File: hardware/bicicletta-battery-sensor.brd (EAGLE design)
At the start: 45.7 x 19.1 mm, 15 parts, among them IC1 LMP92064, IC2 TXB0108

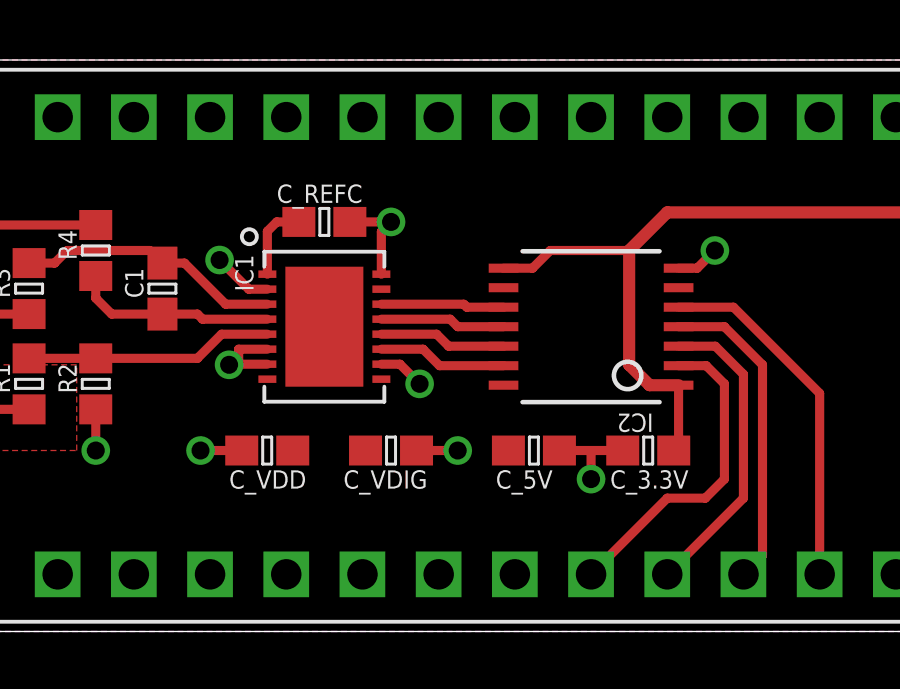
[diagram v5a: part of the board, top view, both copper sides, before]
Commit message: A little more space on the resistors for ease of soldering
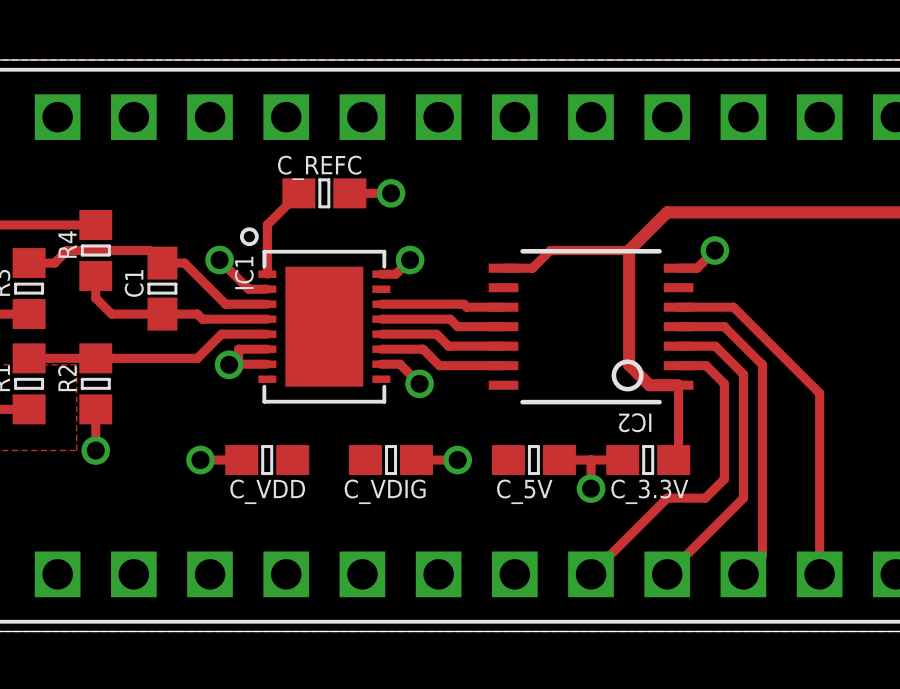
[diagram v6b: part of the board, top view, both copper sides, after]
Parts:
- moved C_REFC 0.95 mm to (19.1, 14.6)
- moved C_3.3V 0.32 mm to (29.8, 5.71)
- moved C_5V 0.32 mm to (26.0, 5.71)
- moved C_VDD 0.32 mm to (17.1, 5.71)
- moved C_VDIG 0.32 mm to (21.3, 5.71)
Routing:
- net REFC: track 2.61 -> 3.13 mm
- net GND: track 18.2 -> 17.9 mm, vias 9 -> 10
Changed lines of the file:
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@@
 <attribute name="VALUE" x="17.05" y="6.16" size="0.8128" layer="27"/>
 </element>
-<element name="C_REFC" library="rcl" package="C0603" value="1uF" x="19.05" y="13.6525" smashed="yes">
-<attribute name="NAME" x="17.4625" y="14.2875" size="0.6096" layer="25"/>
-<attribute name="VALUE" x="18.415" y="11.7475" size="1.27" layer="27"/>
-</element>
-<element name="C_VDD" library="rcl" package="C0603" value="0.1uF" x="17.145" y="6.0325" smashed="yes" rot="R180">
-<attribute name="NAME" x="15.875" y="4.7625" size="0.6096" layer="25"/>
-<attribute name="VALUE" x="17.78" y="7.9375" size="1.27" layer="27" rot="R180"/>
-</element>
-<element name="C_VDIG" library="rcl" package="C0603" value="0.1uF" x="21.2725" y="6.0325" smashed="yes">
-<attribute name="NAME" x="19.685" y="4.7625" size="0.6096" layer="25"/>
-<attribute name="VALUE" x="20.6375" y="4.1275" size="1.27" layer="27"/>
+<element name="C_REFC" library="rcl" package="C0603" value="1uF" x="19.05" y="14.605" smashed="yes">
+<attribute name="NAME" x="17.4625" y="15.24" size="0.6096" layer="25"/>
+<attribute name="VALUE" x="18.415" y="12.7" size="1.27" layer="27"/>
+</element>
+<element name="C_VDD" library="rcl" package="C0603" value="0.1uF" x="17.145" y="5.715" smashed="yes" rot="R180">
+<attribute name="NAME" x="15.875" y="4.445" size="0.6096" layer="25"/>
+<attribute name="VALUE" x="17.78" y="7.62" size="1.27" layer="27" rot="R180"/>
+</element>
+<element name="C_VDIG" library="rcl" package="C0603" value="0.1uF" x="21.2725" y="5.715" smashed="yes">
+<attribute name="NAME" x="19.685" y="4.445" size="0.6096" layer="25"/>
+<attribute name="VALUE" x="20.6375" y="3.81" size="1.27" layer="27"/>
 </element>
 <element name="R3" library="rcl" package="R0603" value="100" x="9.2075" y="11.43" smashed="yes" rot="R90">
@@
 <attribute name="VALUE" x="30.0228" y="14.0462" size="1.016" layer="27" ratio="10" rot="R180"/>
 </element>
-<element name="C_3.3V" library="rcl" package="C0603" value="0.1uF" x="29.845" y="6.0325" smashed="yes" rot="R180">
-<attribute name="NAME" x="28.575" y="4.7625" size="0.6096" layer="25"/>
-<attribute name="VALUE" x="30.48" y="7.9375" size="1.27" layer="27" rot="R180"/>
-</element>
-<element name="C_5V" library="rcl" package="C0603" value="0.1uF" x="26.035" y="6.0325" smashed="yes">
-<attribute name="NAME" x="24.765" y="4.7625" size="0.6096" layer="25"/>
-<attribute name="VALUE" x="25.4" y="4.1275" size="1.27" layer="27"/>
+<element name="C_3.3V" library="rcl" package="C0603" value="0.1uF" x="29.845" y="5.715" smashed="yes" rot="R180">
+<attribute name="NAME" x="28.575" y="4.445" size="0.6096" layer="25"/>
+<attribute name="VALUE" x="30.48" y="7.62" size="1.27" layer="27" rot="R180"/>
+</element>
+<element name="C_5V" library="rcl" package="C0603" value="0.1uF" x="26.035" y="5.715" smashed="yes">
+<attribute name="NAME" x="24.765" y="4.445" size="0.6096" layer="25"/>
+<attribute name="VALUE" x="25.4" y="3.81" size="1.27" layer="27"/>
 </element>
 </elements>
@@
 <wire x1="16.1925" y1="8.91" x2="16.1925" y2="9.41" width="0.3048" layer="1"/>
 <via x="15.875" y="8.89" extent="1-16" drill="0.6"/>
-<via x="14.9225" y="6.0325" extent="1-16" drill="0.6"/>
-<via x="23.495" y="6.0325" extent="1-16" drill="0.6"/>
-<via x="27.94" y="5.08" extent="1-16" drill="0.6"/>
+<via x="14.9225" y="5.715" extent="1-16" drill="0.6"/>
+<via x="23.495" y="5.715" extent="1-16" drill="0.6"/>
+<via x="27.94" y="4.7625" extent="1-16" drill="0.6"/>
 <via x="32.0675" y="12.7" extent="1-16" drill="0.6"/>
-<via x="21.2725" y="13.6525" extent="1-16" drill="0.6"/>
+<via x="21.9075" y="12.3825" extent="1-16" drill="0.6"/>
 <via x="11.43" y="6.0325" extent="1-16" drill="0.6"/>
 <wire x1="11.43" y1="7.405" x2="11.43" y2="6.0325" width="0.3048" layer="1"/>
 <wire x1="16.1925" y1="8.91" x2="15.875" y2="8.91" width="0.3048" layer="1"/>
 <wire x1="15.875" y1="8.91" x2="15.875" y2="8.89" width="0.3048" layer="1"/>
-<wire x1="16.295" y1="6.0325" x2="14.9225" y2="6.0325" width="0.3048" layer="1"/>
-<wire x1="22.1225" y1="6.0325" x2="23.495" y2="6.0325" width="0.3048" layer="1"/>
+<wire x1="16.295" y1="5.715" x2="14.9225" y2="5.715" width="0.3048" layer="1"/>
+<wire x1="22.1225" y1="5.715" x2="23.495" y2="5.715" width="0.3048" layer="1"/>
 <via x="22.225" y="8.255" extent="1-16" drill="0.6"/>
 <wire x1="20.95" y1="8.91" x2="21.57" y2="8.91" width="0.3048" layer="1"/>
 <wire x1="21.57" y1="8.91" x2="22.225" y2="8.255" width="0.3048" layer="1"/>
-<wire x1="26.885" y1="6.0325" x2="27.94" y2="6.0325" width="0.3048" layer="1"/>
-<wire x1="27.94" y1="6.0325" x2="28.995" y2="6.0325" width="0.3048" layer="1"/>
-<wire x1="27.94" y1="5.08" x2="27.94" y2="6.0325" width="0.3048" layer="1"/>
+<wire x1="26.885" y1="5.715" x2="27.94" y2="5.715" width="0.3048" layer="1"/>
+<wire x1="27.94" y1="5.715" x2="28.995" y2="5.715" width="0.3048" layer="1"/>
+<wire x1="27.94" y1="4.7625" x2="27.94" y2="5.715" width="0.3048" layer="1"/>
 <wire x1="30.8578" y1="12.11" x2="31.4775" y2="12.11" width="0.3048" layer="1"/>
 <wire x1="31.4775" y1="12.11" x2="32.0675" y2="12.7" width="0.3048" layer="1"/>
-<wire x1="19.9" y1="13.6525" x2="21.2725" y2="13.6525" width="0.3048" layer="1"/>
-<wire x1="20.95" y1="11.91" x2="20.95" y2="13.33" width="0.3048" layer="1"/>
-<wire x1="20.95" y1="13.33" x2="21.2725" y2="13.6525" width="0.3048" layer="1"/>
+<wire x1="21.585" y1="12.06" x2="21.9075" y2="12.3825" width="0.3048" layer="1"/>
 <via x="15.5575" y="12.3825" extent="1-16" drill="0.6"/>
 <wire x1="17.15" y1="11.41" x2="16.53" y2="11.41" width="0.3048" layer="1"/>
 <wire x1="16.53" y1="11.41" x2="15.5575" y2="12.3825" width="0.3048" layer="1"/>
+<via x="21.2725" y="14.605" extent="1-16" drill="0.6"/>
+<wire x1="19.9" y1="14.605" x2="21.2725" y2="14.605" width="0.3048" layer="1"/>
+<wire x1="20.95" y1="11.91" x2="21.435" y2="11.91" width="0.3048" layer="1"/>
+<wire x1="21.435" y1="11.91" x2="21.9075" y2="12.3825" width="0.3048" layer="1"/>
+<wire x1="32.0675" y1="12.7" x2="43.18" y2="17.145" width="0" layer="19" extent="1-1"/>
+<wire x1="28.995" y1="5.715" x2="30.8578" y2="12.11" width="0" layer="19" extent="1-1"/>
+<wire x1="23.495" y1="5.715" x2="26.885" y2="5.715" width="0" layer="19" extent="1-1"/>
+<wire x1="22.225" y1="8.255" x2="22.1225" y2="5.715" width="0" layer="19" extent="1-1"/>
+<wire x1="20.95" y1="11.91" x2="20.95" y2="8.91" width="0" layer="19" extent="1-1"/>
+<wire x1="21.2725" y1="14.605" x2="21.9075" y2="12.3825" width="0" layer="19" extent="1-1"/>
+<wire x1="17.15" y1="8.91" x2="20.95" y2="8.91" width="0" layer="19" extent="1-1"/>
+<wire x1="17.15" y1="11.41" x2="17.15" y2="9.41" width="0" layer="19" extent="1-1"/>
+<wire x1="16.295" y1="5.715" x2="16.1925" y2="8.91" width="0" layer="19" extent="1-1"/>
+<wire x1="11.43" y1="6.0325" x2="14.9225" y2="5.715" width="0" layer="19" extent="1-1"/>
+<wire x1="3.81" y1="13.335" x2="11.43" y2="7.405" width="0" layer="19" extent="1-1"/>
+<wire x1="40.64" y1="1.905" x2="28.995" y2="5.715" width="0" layer="19" extent="1-1"/>
+<wire x1="43.18" y1="1.905" x2="40.64" y2="1.905" width="0" layer="19" extent="1-1"/>
 </signal>
 <signal name="V_BATT">
@@
 <contactref element="C_3.3V" pad="1"/>
 <wire x1="30.8578" y1="8.21" x2="30.8578" y2="6.1953" width="0.3048" layer="1"/>
-<wire x1="30.8578" y1="6.1953" x2="30.695" y2="6.0325" width="0.3048" layer="1"/>
+<wire x1="30.8578" y1="6.1953" x2="30.695" y2="5.715" width="0.3048" layer="1"/>
 <wire x1="25.0222" y1="12.11" x2="25.99" y2="12.11" width="0.3048" layer="1"/>
 <wire x1="40.64" y1="17.145" x2="40.64" y2="15.24" width="0.4064" layer="1"/>
@@
 <contactref element="IC1" pad="P$1"/>
 <contactref element="C_REFC" pad="1"/>
-<wire x1="17.15" y1="11.91" x2="17.15" y2="13.34" width="0.3048" layer="1"/>
-<wire x1="17.15" y1="13.34" x2="17.4625" y2="13.6525" width="0.3048" layer="1"/>
-<wire x1="18.2" y1="13.6525" x2="17.4625" y2="13.6525" width="0.3048" layer="1"/>
+<wire x1="17.15" y1="11.91" x2="17.15" y2="13.555" width="0.3048" layer="1"/>
+<wire x1="17.15" y1="13.555" x2="18.2" y2="14.605" width="0.3048" layer="1"/>
 </signal>
 <signal name="N$3">
@@
 </signal>
 </signals>
-<errors>
-</errors>
 </board>
 </drawing>
